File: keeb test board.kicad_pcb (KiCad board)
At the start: 2 copper layers, 60 x 100 mm, 60 parts, among them SW1 SW_Push, SW10 SW_Push, SW11 SW_Push, SW12 SW_Push, SW13 SW_Push, SW14 SW_Push, SW15 SW_Push, SW2 SW_Push, SW3 SW_Push, SW4 SW_Push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

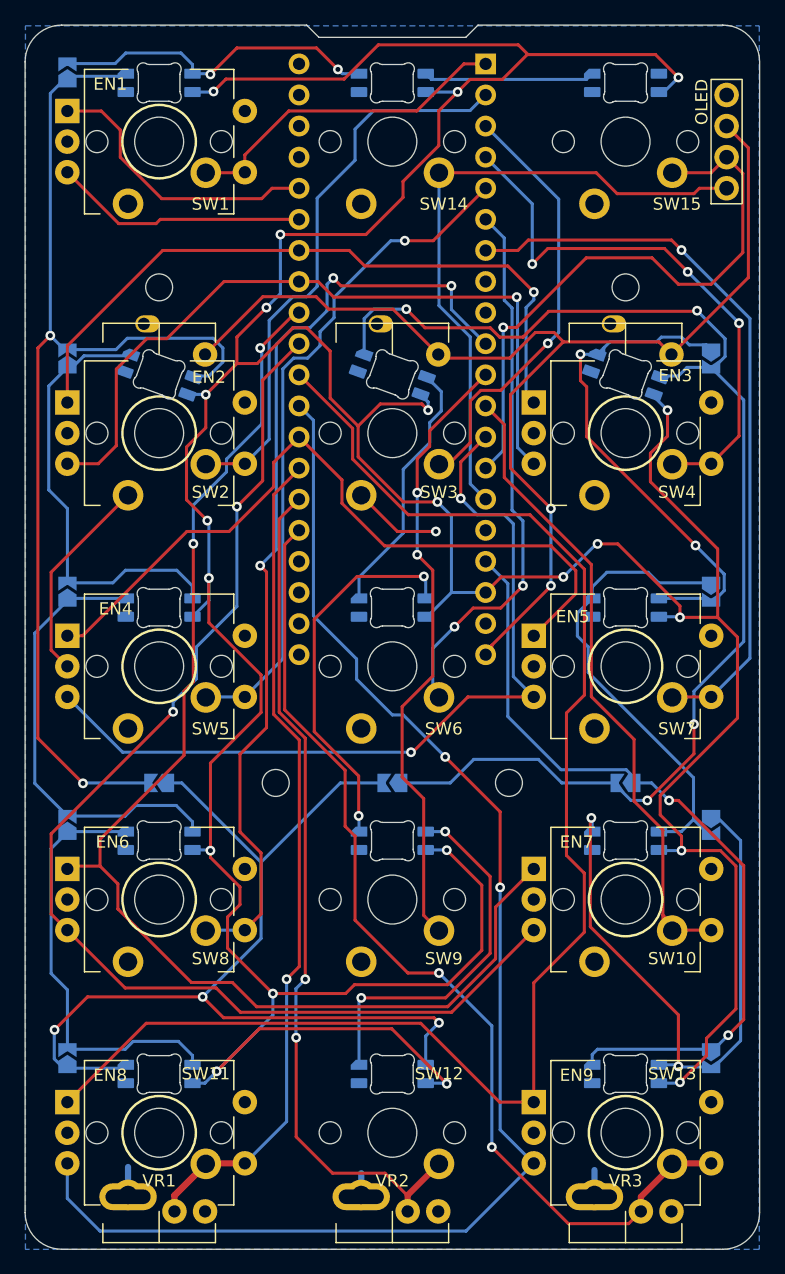
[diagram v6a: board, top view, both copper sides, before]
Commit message: routing and silkscreen improvements
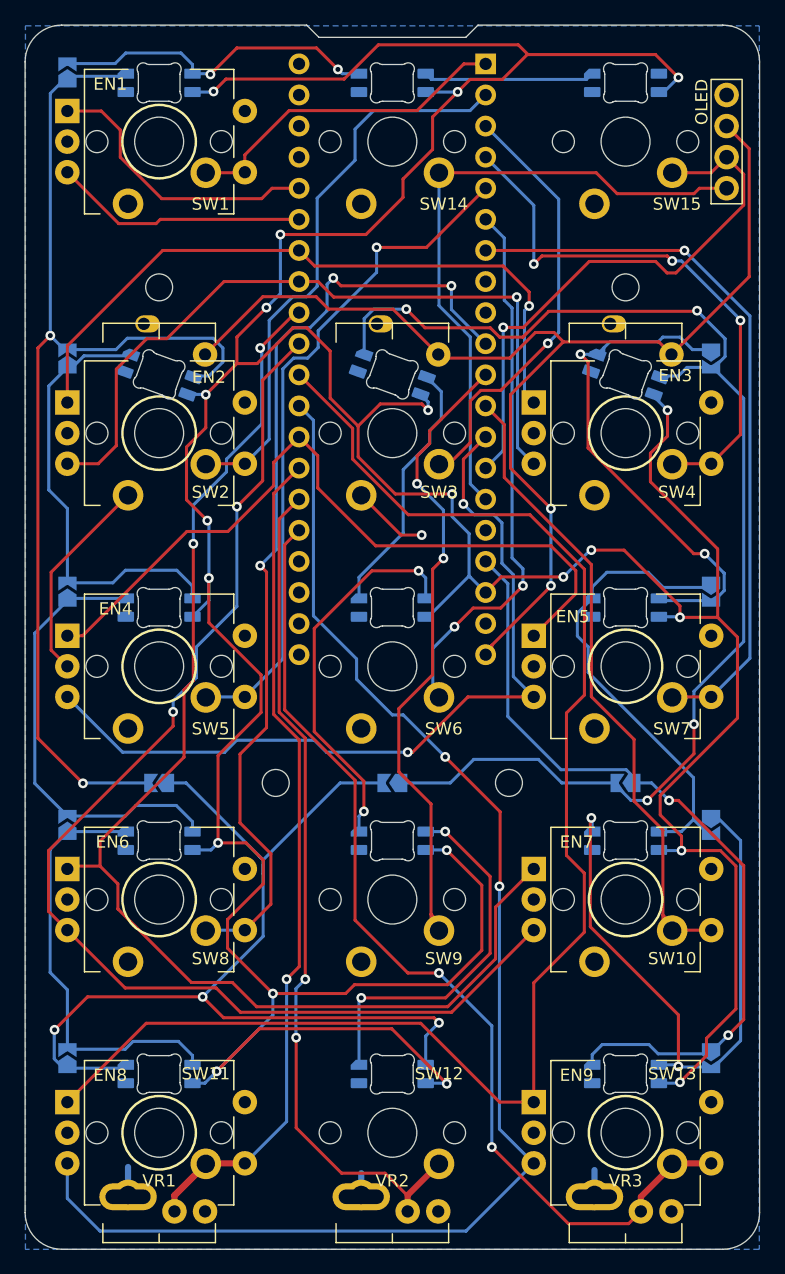
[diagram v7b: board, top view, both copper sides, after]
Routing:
- net +5V: track 366.1 -> 370.8 mm
- net SCL-SW: track 49.3 -> 46.1 mm
- net KEY9: track 50.5 -> 52.5 mm
- net Net-(D8-Pad2): track 81.9 -> 83.0 mm
- net GND: track 30.5 -> 29.5 mm
- net KEY8: track 77.9 -> 78.6 mm
- net LED_DATA: track 64.5 -> 65.2 mm
- net KEY7: track 60.0 -> 59.4 mm
- net Net-(D3-Pad2): track 42.1 -> 42.6 mm

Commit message: routing and footprint fixes
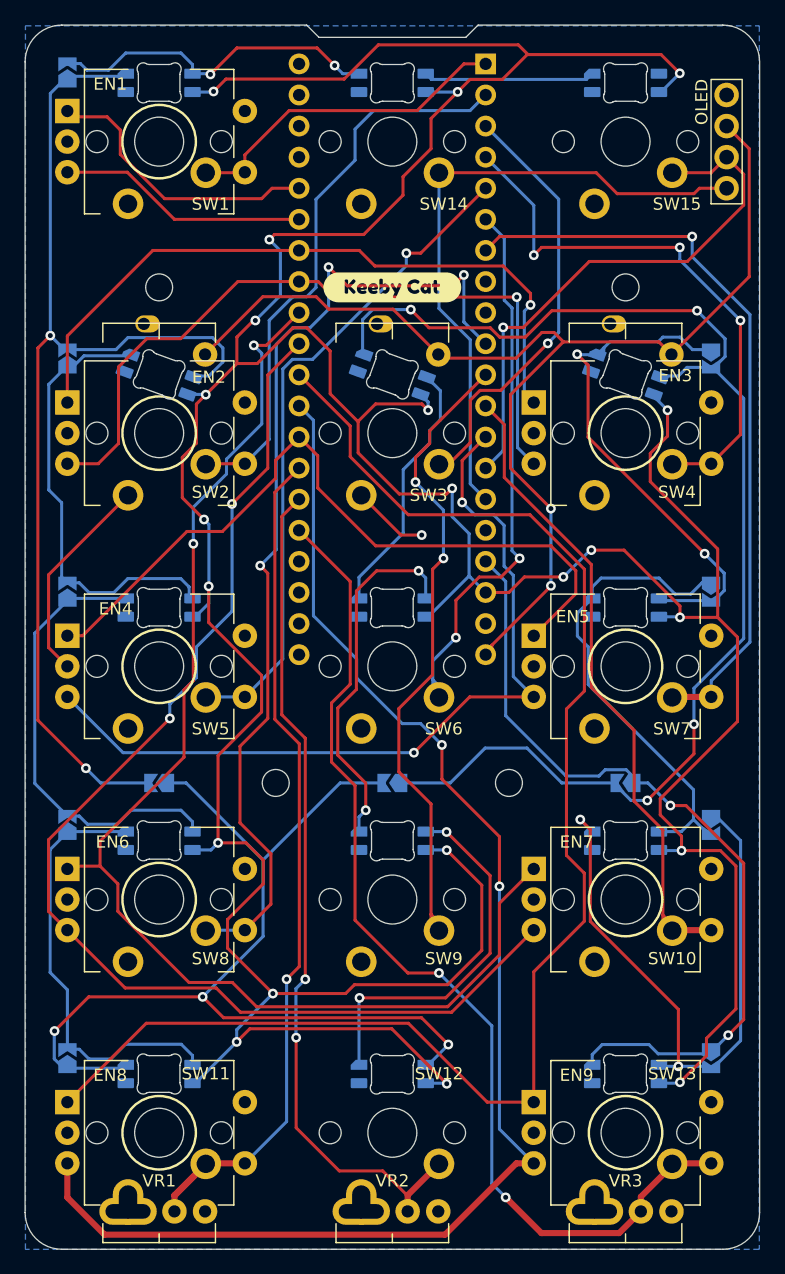
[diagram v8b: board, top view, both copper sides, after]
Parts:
- added kibuzzard-6226FF10: G***, kibuzzard-6226FF10, F.Cu at (92.2, 78.5)
- added kibuzzard-6226FF10: G***, kibuzzard-6226FF10, B.Cu at (110.8, 136.9)
- added kibuzzard-6227022E: G***, kibuzzard-6227022E, B.Cu at (92.2, 78.5)
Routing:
- net GND: track 29.5 -> 23.6 mm
- net KEY8: track 78.6 -> 82.0 mm
- net KEY13-POT3: track 82.6 -> 85.3 mm
- net KEY7: track 59.4 -> 61.4 mm
- net +5V: track 370.8 -> 368.8 mm
- net Net-(D6-Pad2): track 31.4 -> 29.7 mm
- net KEY5: track 55.9 -> 54.5 mm
- net KEY6: track 44.2 -> 45.3 mm
- net ENC4A: track 103.5 -> 104.5 mm
- net Net-(D8-Pad2): track 83.0 -> 82.1 mm
- net Net-(D12-Pad2): track 90.0 -> 89.1 mm
- net SCL-SW: track 46.1 -> 45.3 mm
- net Net-(D4-Pad2): track 105.2 -> 106.0 mm
- net ENC3B: track 68.0 -> 67.2 mm
- net LED_DATA: track 65.2 -> 65.8 mm
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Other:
- board text added: "V${revision}"
- board text added: "©Cole Morris 2022"
- board text removed: "Blue Pill"
- board text removed: "Keeby Cat V${revision} © COLE MORRIS 2022"
